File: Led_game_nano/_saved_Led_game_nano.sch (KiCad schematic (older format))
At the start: 36 parts

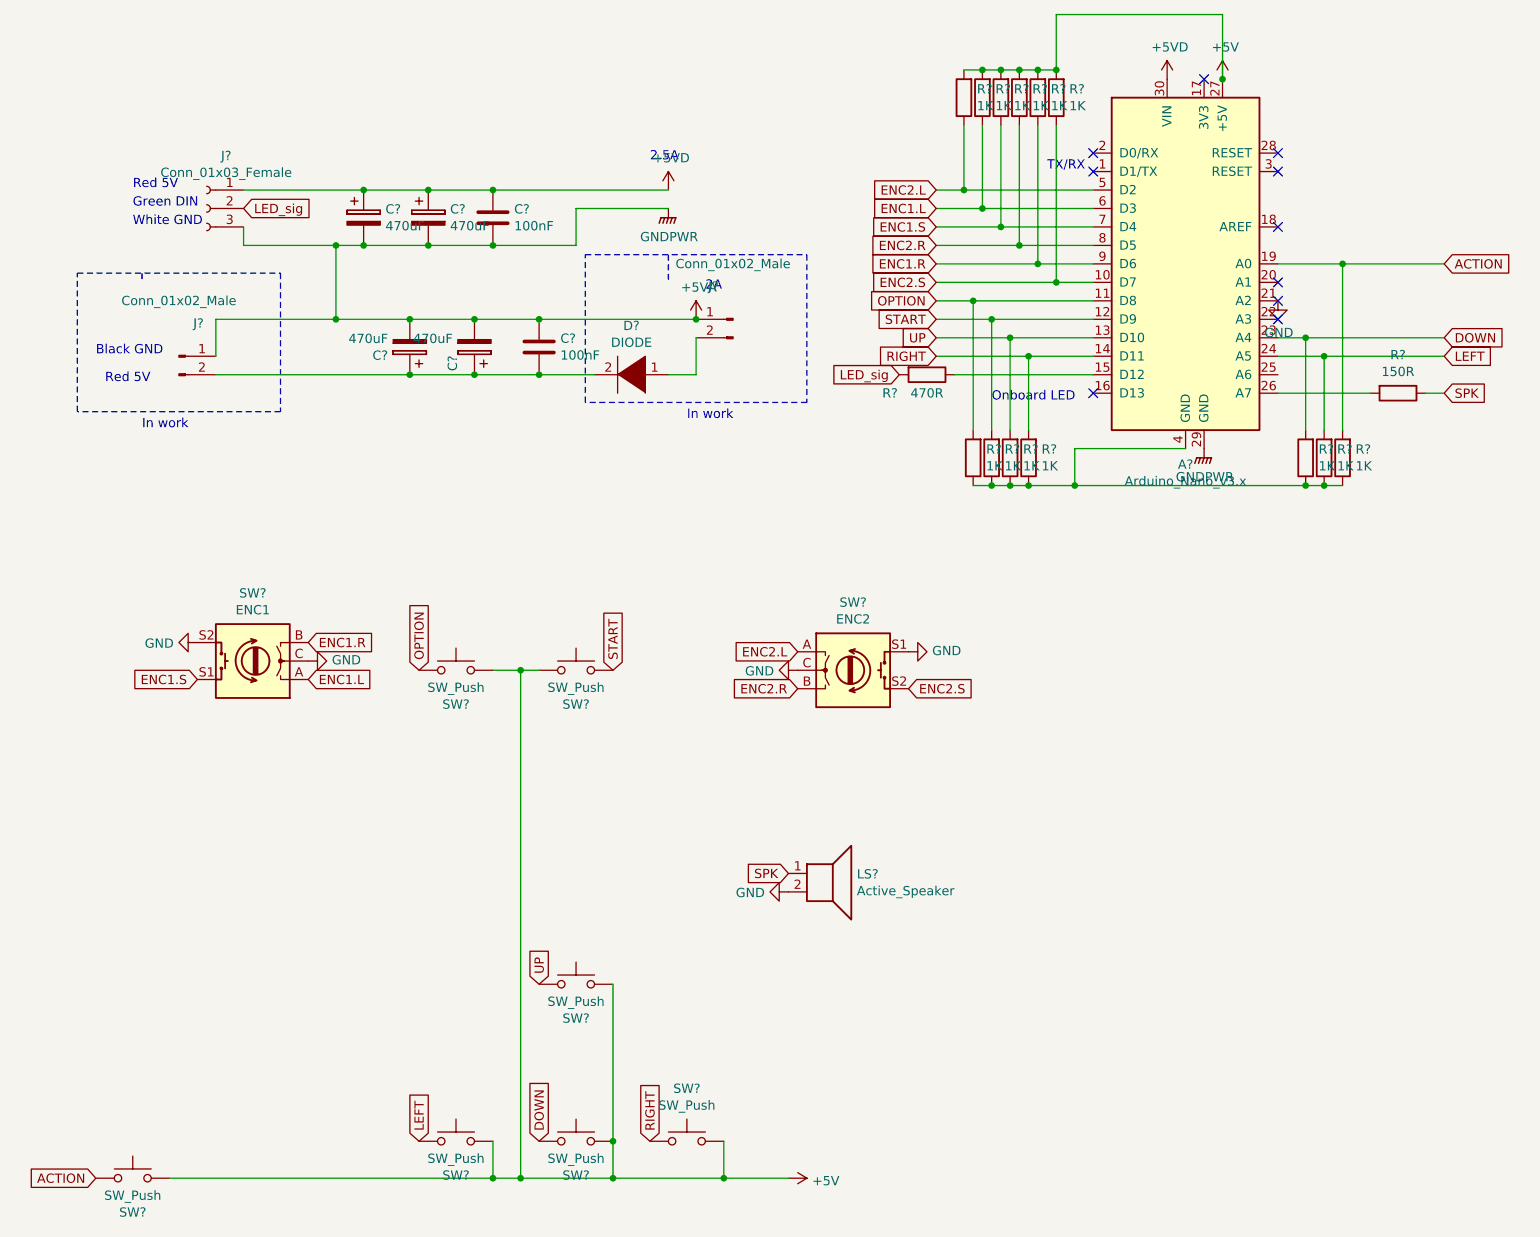
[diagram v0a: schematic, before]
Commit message: Buttons are working
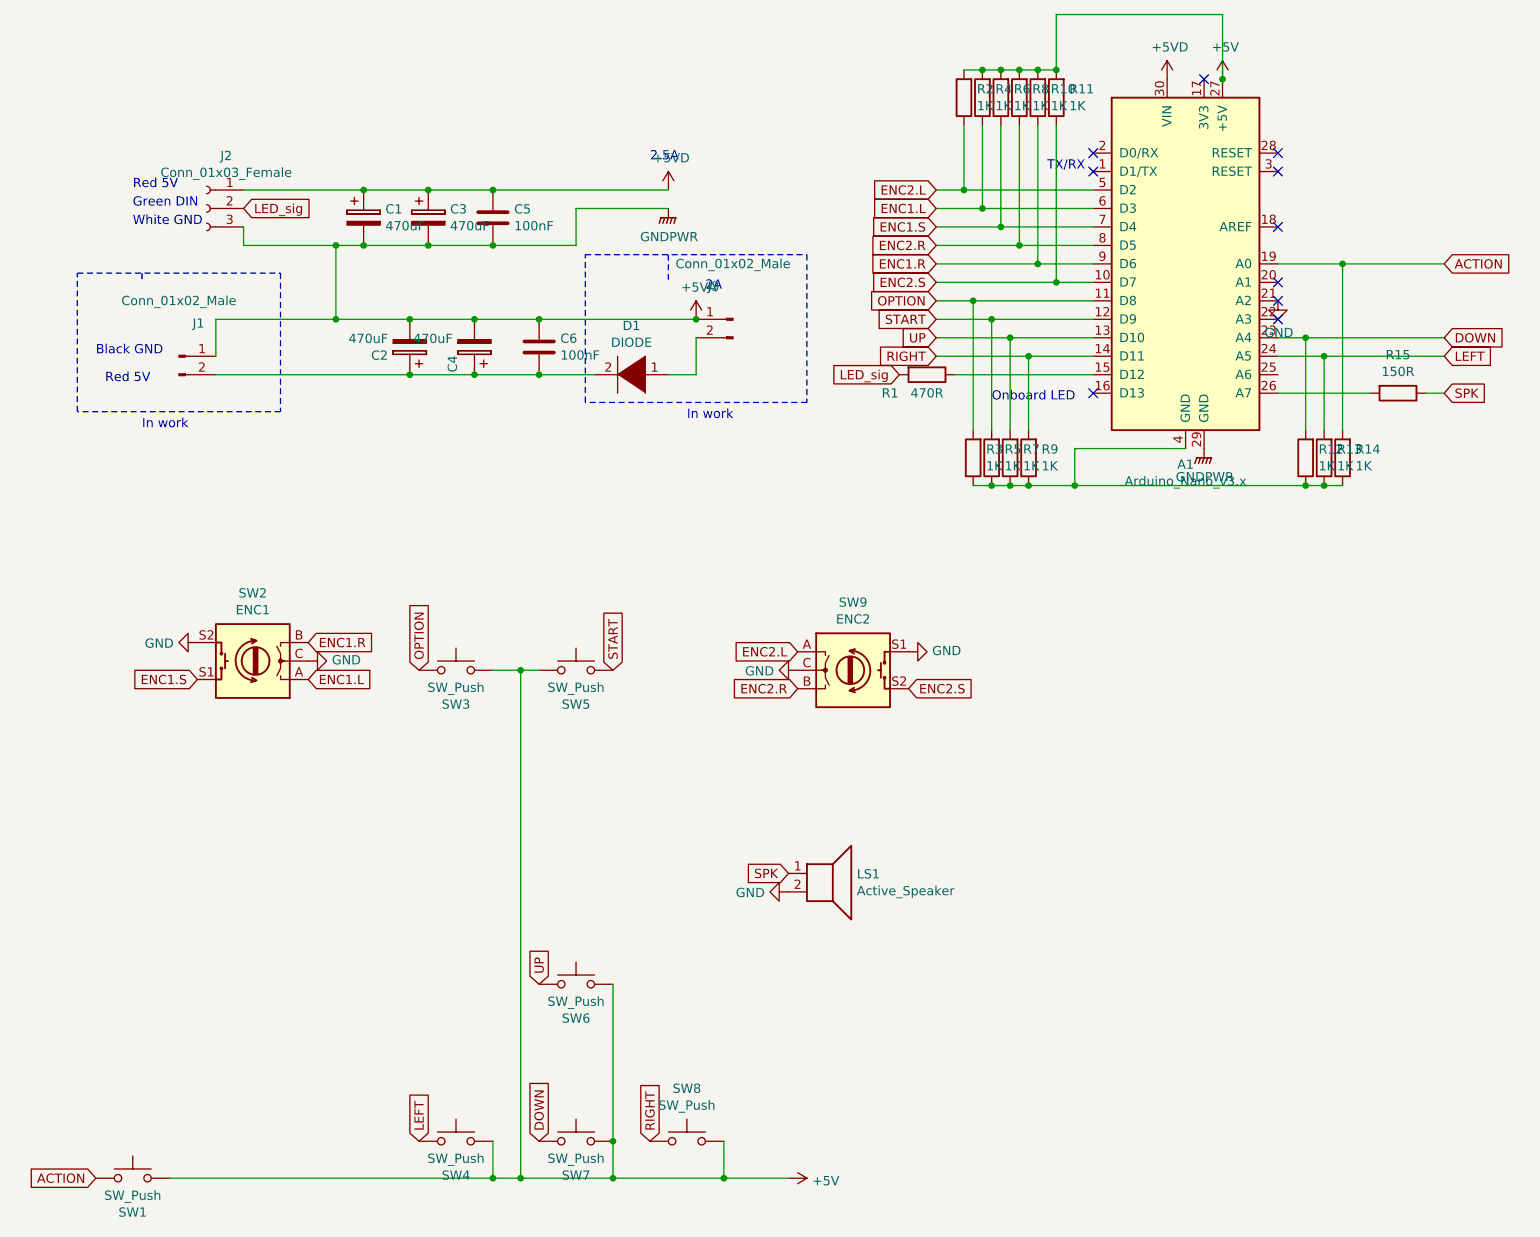
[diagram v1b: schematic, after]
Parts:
- gave numbers to parts that had none: 36
